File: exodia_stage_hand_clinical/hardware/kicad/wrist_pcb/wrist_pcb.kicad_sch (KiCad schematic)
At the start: 16 parts, among them J1 USBC_16PIN, J2 ZIF_5PIN, Q1 AO3400A, Q2 2N7002, Q3 2N7002, Q4 2N7002, Q5 2N7002, U1 ESP32S3_MODULE, U2 TP4056_IC, U3 AP2112K

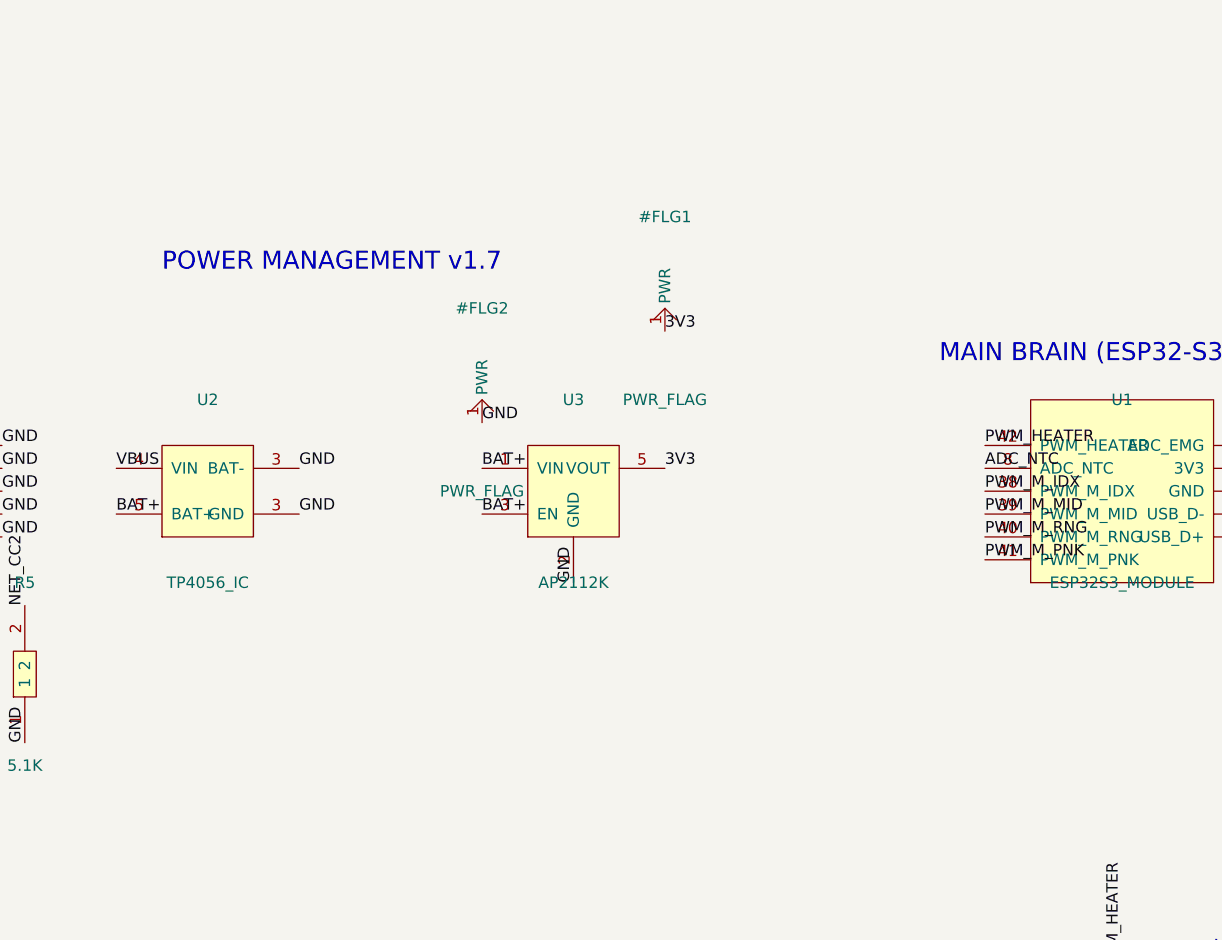
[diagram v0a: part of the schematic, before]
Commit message: Schematic v1.8: Decoupling Capacitors (TP4056, LDO, ESP32)
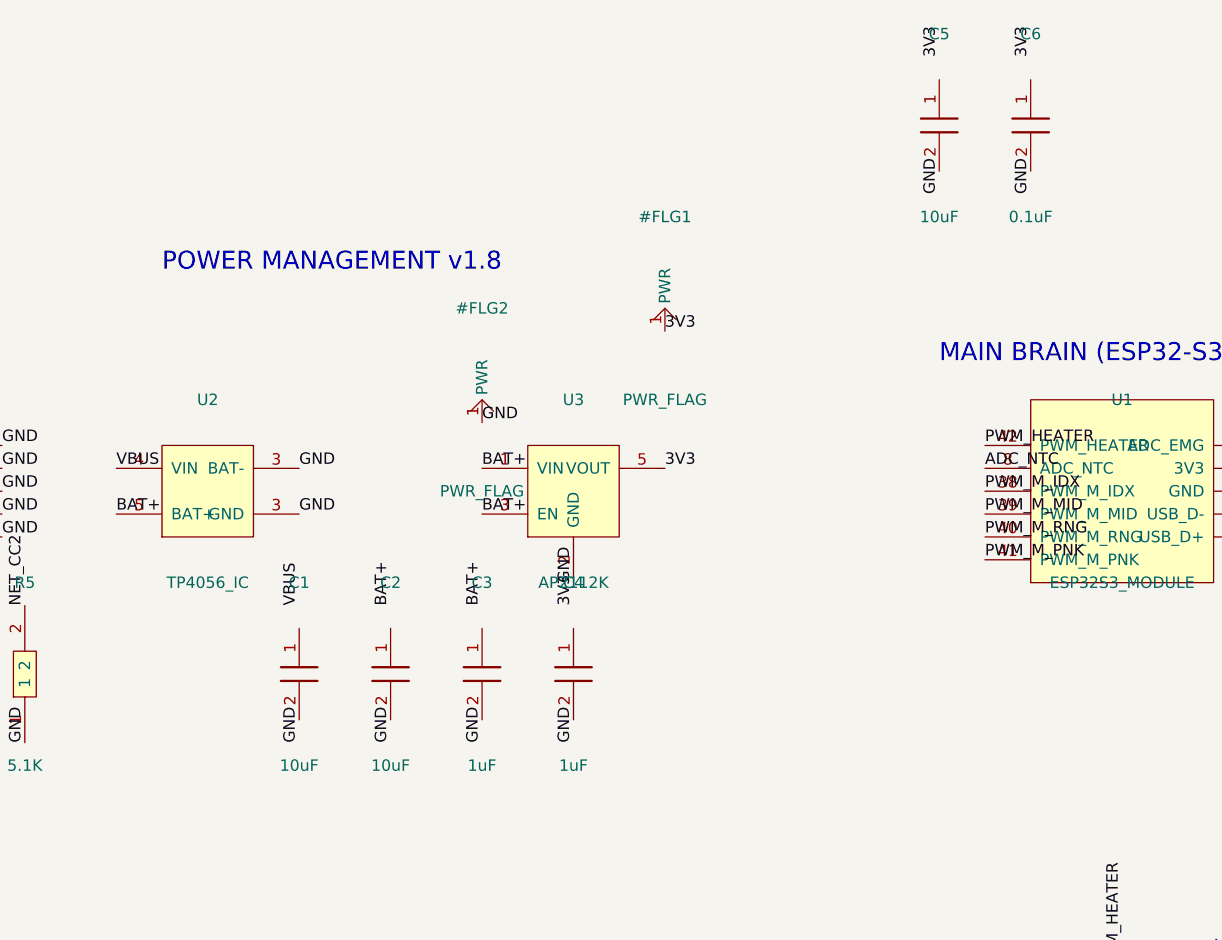
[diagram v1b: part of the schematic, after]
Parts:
- added C1, C2, C5: 10uF, symbol CAPACITOR
- added C3, C4: 1uF, symbol CAPACITOR
- added C6: 0.1uF, symbol CAPACITOR
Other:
- note added: "POWER MANAGEMENT v1.8"
- note removed: "POWER MANAGEMENT v1.7"
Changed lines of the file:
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@@
     (title "Exodia Stage Hand - Clinical Wrist PCB")
     (date "2026-05-16")
-    (rev "v1.7")
+    (rev "v1.8")
     (company "Resonanx")
   )
@@
     (property "Datasheet" "" (id 3) (at 101.6 157.48 0) (effects (hide yes)))
   )
+  (symbol (lib_id "CAPACITOR") (at 60.96 96.52 0) (unit 1) (in_bom yes) (on_board yes)
+    (property "Reference" "C1" (id 0) (at 60.96 86.36 0) (effects (font (size 1.27 1.27))))
+    (property "Value" "10uF" (id 1) (at 60.96 106.67999999999999 0) (effects (font (size 1.27 1.27))))
+    (property "Footprint" "" (id 2) (at 60.96 96.52 0) (effects (hide yes)))
+    (property "Datasheet" "" (id 3) (at 60.96 96.52 0) (effects (hide yes)))
+  )
+  (symbol (lib_id "CAPACITOR") (at 71.12 96.52 0) (unit 1) (in_bom yes) (on_board yes)
+    (property "Reference" "C2" (id 0) (at 71.12 86.36 0) (effects (font (size 1.27 1.27))))
+    (property "Value" "10uF" (id 1) (at 71.12 106.67999999999999 0) (effects (font (size 1.27 1.27))))
+    (property "Footprint" "" (id 2) (at 71.12 96.52 0) (effects (hide yes)))
+    (property "Datasheet" "" (id 3) (at 71.12 96.52 0) (effects (hide yes)))
+  )
+  (symbol (lib_id "CAPACITOR") (at 81.28 96.52 0) (unit 1) (in_bom yes) (on_board yes)
+    (property "Reference" "C3" (id 0) (at 81.28 86.36 0) (effects (font (size 1.27 1.27))))
+    (property "Value" "1uF" (id 1) (at 81.28 106.67999999999999 0) (effects (font (size 1.27 1.27))))
+    (property "Footprint" "" (id 2) (at 81.28 96.52 0) (effects (hide yes)))
+    (property "Datasheet" "" (id 3) (at 81.28 96.52 0) (effects (hide yes)))
+  )
+  (symbol (lib_id "CAPACITOR") (at 91.44 96.52 0) (unit 1) (in_bom yes) (on_board yes)
+    (property "Reference" "C4" (id 0) (at 91.44 86.36 0) (effects (font (size 1.27 1.27))))
+    (property "Value" "1uF" (id 1) (at 91.44 106.67999999999999 0) (effects (font (size 1.27 1.27))))
+    (property "Footprint" "" (id 2) (at 91.44 96.52 0) (effects (hide yes)))
+    (property "Datasheet" "" (id 3) (at 91.44 96.52 0) (effects (hide yes)))
+  )
+  (symbol (lib_id "CAPACITOR") (at 132.08 35.56 0) (unit 1) (in_bom yes) (on_board yes)
+    (property "Reference" "C5" (id 0) (at 132.08 25.400000000000002 0) (effects (font (size 1.27 1.27))))
+    (property "Value" "10uF" (id 1) (at 132.08 45.72 0) (effects (font (size 1.27 1.27))))
+    (property "Footprint" "" (id 2) (at 132.08 35.56 0) (effects (hide yes)))
+    (property "Datasheet" "" (id 3) (at 132.08 35.56 0) (effects (hide yes)))
+  )
+  (symbol (lib_id "CAPACITOR") (at 142.24 35.56 0) (unit 1) (in_bom yes) (on_board yes)
+    (property "Reference" "C6" (id 0) (at 142.24 25.400000000000002 0) (effects (font (size 1.27 1.27))))
+    (property "Value" "0.1uF" (id 1) (at 142.24 45.72 0) (effects (font (size 1.27 1.27))))
+    (property "Footprint" "" (id 2) (at 142.24 35.56 0) (effects (hide yes)))
+    (property "Datasheet" "" (id 3) (at 142.24 35.56 0) (effects (hide yes)))
+  )
   (symbol (lib_id "PWR_FLAG") (at 101.6 55.88 0) (unit 1) (in_bom yes) (on_board yes)
     (property "Reference" "#FLG1" (id 0) (at 101.6 45.72 0) (effects (font (size 1.27 1.27))))
@@
     (property "Datasheet" "" (id 3) (at 81.28 66.04 0) (effects (hide yes)))
   )
-  (text "POWER MANAGEMENT v1.7" (at 45.72 50.8 0) (effects (font (size 2 2)) (justify left)))
+  (text "POWER MANAGEMENT v1.8" (at 45.72 50.8 0) (effects (font (size 2 2)) (justify left)))
   (text "MAIN BRAIN (ESP32-S3)" (at 132.08 60.96 0) (effects (font (size 2 2)) (justify left)))
   (text "HEATER MOSFET" (at 162.56 127 0) (effects (font (size 1.5 1.5)) (justify left)))
@@
   (label "NET_M_MID" (at 223.52 139.7 180) (effects (font (size 1.27 1.27)) (justify left bottom)))
   (label "NET_M_RNG_PNK" (at 223.52 142.24 180) (effects (font (size 1.27 1.27)) (justify left bottom)))
+  (label "VBUS" (at 60.96 88.89999999999999 90) (effects (font (size 1.27 1.27)) (justify left bottom)))
+  (label "GND" (at 60.96 104.14 270) (effects (font (size 1.27 1.27)) (justify left bottom)))
+  (label "BAT+" (at 71.12 88.89999999999999 90) (effects (font (size 1.27 1.27)) (justify left bottom)))
+  (label "GND" (at 71.12 104.14 270) (effects (font (size 1.27 1.27)) (justify left bottom)))
+  (label "BAT+" (at 81.28 88.89999999999999 90) (effects (font (size 1.27 1.27)) (justify left bottom)))
+  (label "GND" (at 81.28 104.14 270) (effects (font (size 1.27 1.27)) (justify left bottom)))
+  (label "3V3" (at 91.44 88.89999999999999 90) (effects (font (size 1.27 1.27)) (justify left bottom)))
+  (label "GND" (at 91.44 104.14 270) (effects (font (size 1.27 1.27)) (justify left bottom)))
+  (label "3V3" (at 132.08 27.94 90) (effects (font (size 1.27 1.27)) (justify left bottom)))
+  (label "GND" (at 132.08 43.18 270) (effects (font (size 1.27 1.27)) (justify left bottom)))
+  (label "3V3" (at 142.24 27.94 90) (effects (font (size 1.27 1.27)) (justify left bottom)))
+  (label "GND" (at 142.24 43.18 270) (effects (font (size 1.27 1.27)) (justify left bottom)))
   (label "3V3" (at 101.6 58.42 0) (effects (font (size 1.27 1.27)) (justify left bottom)))
   (label "GND" (at 81.28 68.58000000000001 0) (effects (font (size 1.27 1.27)) (justify left bottom)))

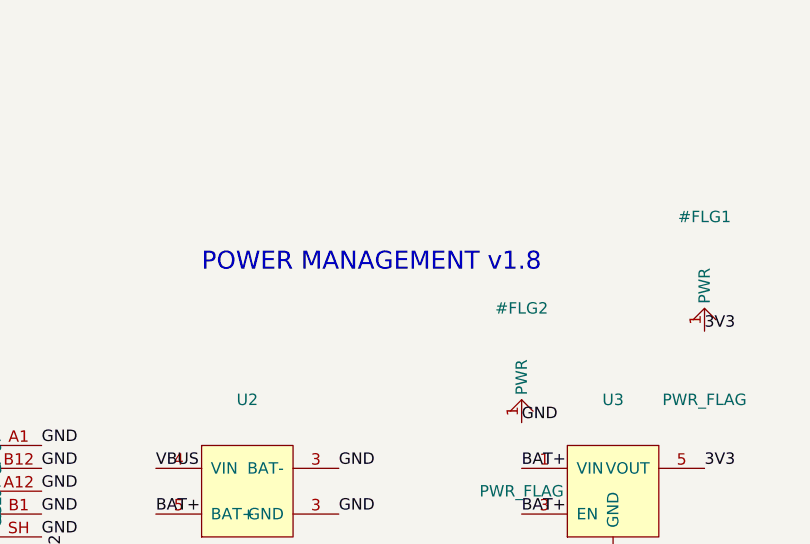
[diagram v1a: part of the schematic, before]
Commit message: Schematic v1.9: Re-mapped motor and heater gates to right-facing GPIOs (21-25) for optimized PCB routing
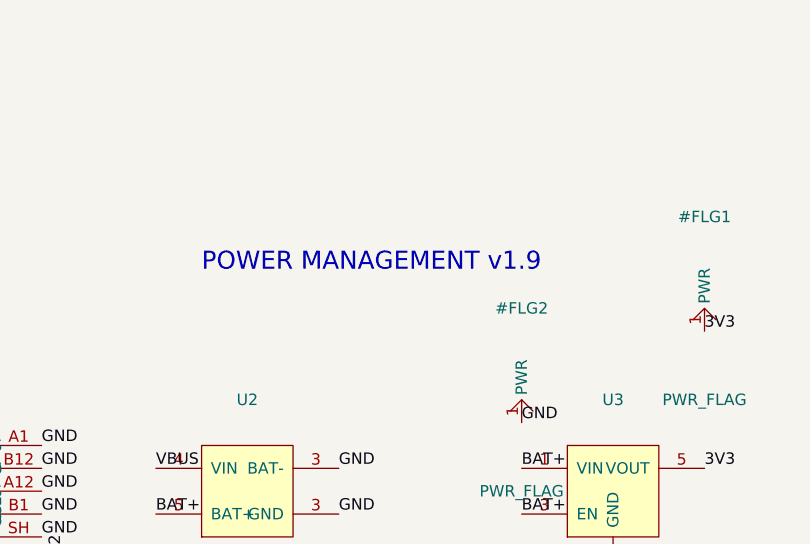
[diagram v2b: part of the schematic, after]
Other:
- note added: "POWER MANAGEMENT v1.9"
- note removed: "POWER MANAGEMENT v1.8"
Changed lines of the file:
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@@
     (title "Exodia Stage Hand - Clinical Wrist PCB")
     (date "2026-05-16")
-    (rev "v1.8")
+    (rev "v1.9")
     (company "Resonanx")
   )
@@
     (property "Datasheet" "" (id 3) (at 81.28 66.04 0) (effects (hide yes)))
   )
-  (text "POWER MANAGEMENT v1.8" (at 45.72 50.8 0) (effects (font (size 2 2)) (justify left)))
+  (text "POWER MANAGEMENT v1.9" (at 45.72 50.8 0) (effects (font (size 2 2)) (justify left)))
   (text "MAIN BRAIN (ESP32-S3)" (at 132.08 60.96 0) (effects (font (size 2 2)) (justify left)))
   (text "HEATER MOSFET" (at 162.56 127 0) (effects (font (size 1.5 1.5)) (justify left)))

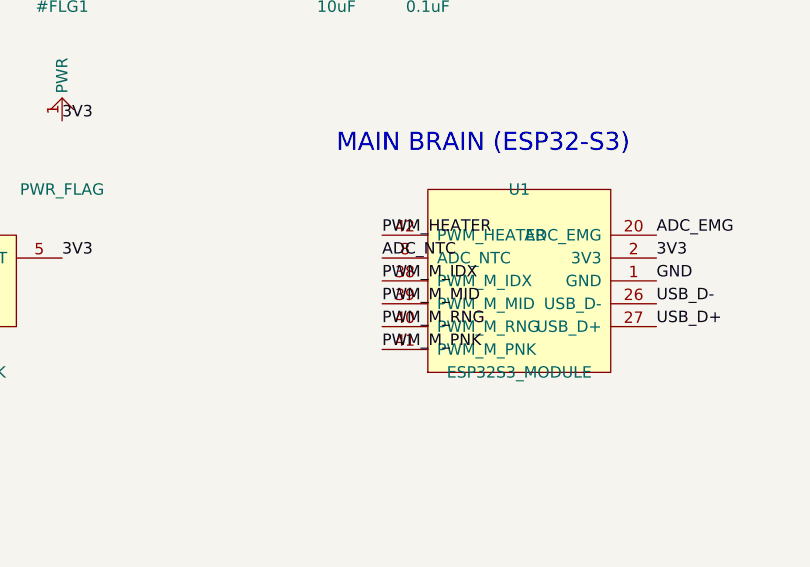
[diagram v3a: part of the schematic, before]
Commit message: Schematic v1.9: Fixed Python code replacement bug and correctly re-mapped pins to 21-25
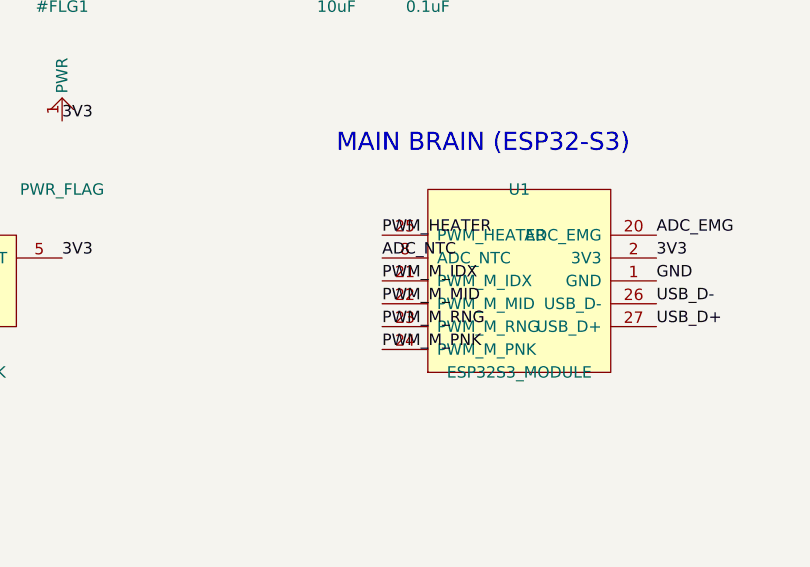
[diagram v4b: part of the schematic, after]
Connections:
- net PWM_HEATER: now also U1.25 (PWM_HEATER); no longer U1.42 (PWM_HEATER)
- net PWM_M_IDX: now also U1.21 (PWM_M_IDX); no longer U1.38 (PWM_M_IDX)
- net PWM_M_MID: now also U1.22 (PWM_M_MID); no longer U1.39 (PWM_M_MID)
- net PWM_M_PNK: now also U1.24 (PWM_M_PNK); no longer U1.41 (PWM_M_PNK)
- net PWM_M_RNG: now also U1.23 (PWM_M_RNG); no longer U1.40 (PWM_M_RNG)

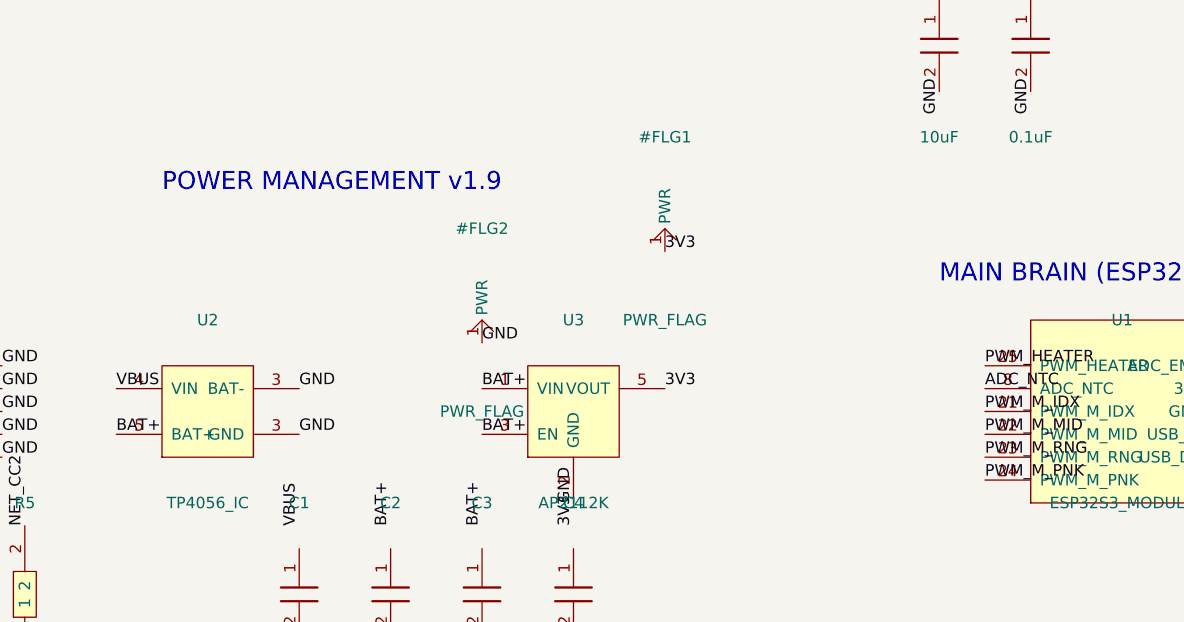
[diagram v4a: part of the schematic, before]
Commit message: Schematic v1.10: Reverted Q4 (PWM_M_RNG) back to Pin 40 to preserve active trace, other pins kept on safe 21-25
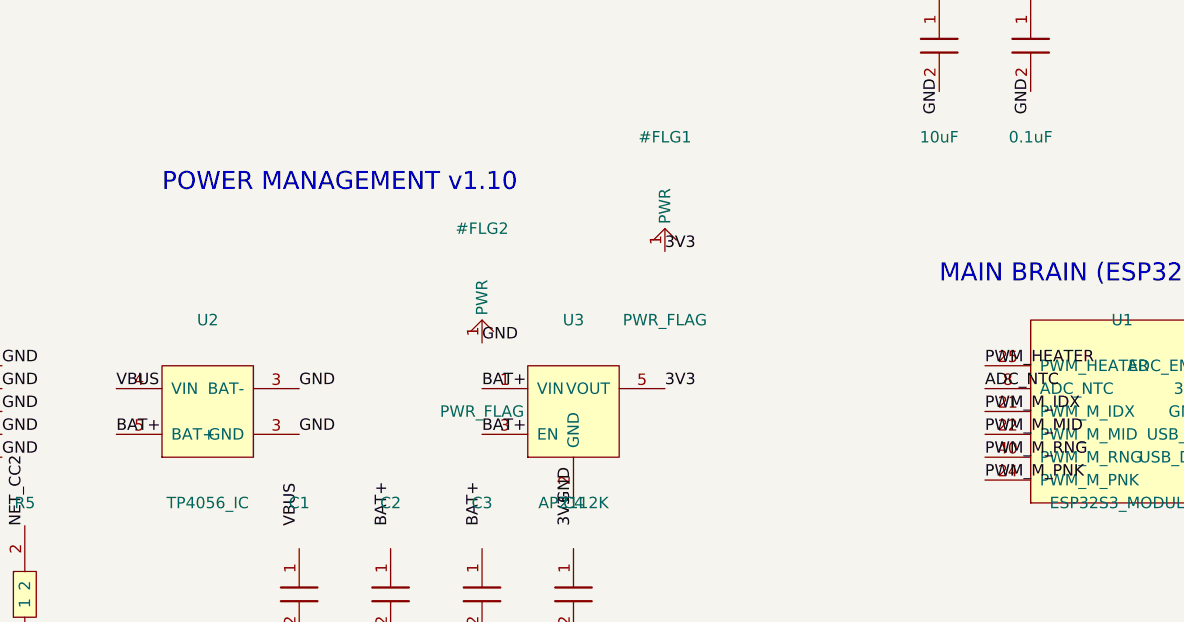
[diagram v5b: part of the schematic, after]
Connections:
- net PWM_M_RNG: now also U1.40 (PWM_M_RNG); no longer U1.23 (PWM_M_RNG)
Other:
- note added: "POWER MANAGEMENT v1.10"
- note removed: "POWER MANAGEMENT v1.9"
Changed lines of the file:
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@@
     (title "Exodia Stage Hand - Clinical Wrist PCB")
     (date "2026-05-16")
-    (rev "v1.9")
+    (rev "v1.10")
     (company "Resonanx")
   )
@@
     (property "Datasheet" "" (id 3) (at 81.28 66.04 0) (effects (hide yes)))
   )
-  (text "POWER MANAGEMENT v1.9" (at 45.72 50.8 0) (effects (font (size 2 2)) (justify left)))
+  (text "POWER MANAGEMENT v1.10" (at 45.72 50.8 0) (effects (font (size 2 2)) (justify left)))
   (text "MAIN BRAIN (ESP32-S3)" (at 132.08 60.96 0) (effects (font (size 2 2)) (justify left)))
   (text "HEATER MOSFET" (at 162.56 127 0) (effects (font (size 1.5 1.5)) (justify left)))

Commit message: Add Exodia Wrist PCB Rev B and update schematic/layout; clean up .history submodule and optimize .gitignore for KiCad
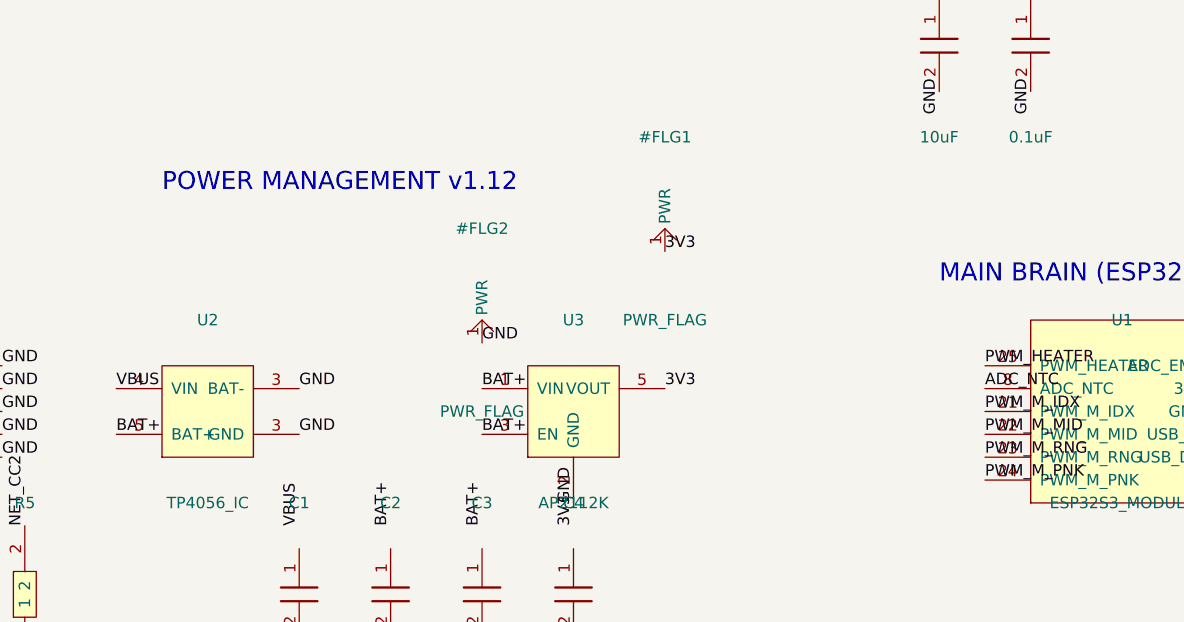
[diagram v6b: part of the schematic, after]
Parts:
- C1, C2, C3, C4, C5, C6: footprint (none) -> Capacitor_SMD:C_0603_1608Metric
- J1: footprint (none) -> Connector_USB:USB_C_Receptacle_XKB_U262-16XN-4BVC11
- J2: footprint (none) -> Connector_FFC-FPC:TE_0-1734839-5_1x05-1MP_P0.5mm_Horizontal
- Q1, Q2, Q3, Q4, Q5: footprint (none) -> Package_TO_SOT_SMD:SOT-23-3
- R1, R2, R3, R4, R5, RT1: footprint (none) -> Resistor_SMD:R_0603_1608Metric
- U1: footprint (none) -> RF_Module:ESP32-S2-MINI-1
- U2: footprint (none) -> Package_SO:SOIC-8-1EP_3.9x4.9mm_P1.27mm_EP2.29x3mm_ThermalVias
- U3: footprint (none) -> Package_TO_SOT_SMD:SOT-23-5
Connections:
- net PWM_M_RNG: now also U1.23 (PWM_M_RNG); no longer U1.40 (PWM_M_RNG)
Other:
- note added: "POWER MANAGEMENT v1.12"
- note removed: "POWER MANAGEMENT v1.10"
